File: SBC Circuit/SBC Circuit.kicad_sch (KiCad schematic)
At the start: 21 parts, among them J3 Conn_01x06_Pin, SW1 RESET, U1 MC68000FN, U11 MC34064P, X1 SG-531

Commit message: Assign Footprints
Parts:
- C10, C11, C12, C13, C14, C15, C5, C6, C7, C8, C9: footprint (none) -> Capacitor_THT:CP_Box_L5.50mm_W4.00mm_P2.50mm_NonPolarized
- J3: footprint (none) -> Connector_PinHeader_2.54mm:PinHeader_1x06_P2.54mm_Vertical
- R2, R3, R4: footprint (none) -> Resistor_THT:R_Axial_DIN0204_L3.6mm_D1.6mm_P2.54mm_Vertical
- SW1: footprint (none) -> Button_Switch_THT:SW_PUSH_6mm
- TP3: footprint (none) -> TestPoint:TestPoint_Keystone_5000-5004_Miniature
- U1: footprint Package_LCC:PLCC-68 -> Package_LCC:PLCC-68_THT-Socket
- U11: footprint Package_TO_SOT_THT:TO-92L_Inline -> Package_TO_SOT_THT:TO-92_Inline
- U2: value ~ -> XC9572XL; footprint (none) -> Package_LCC:PLCC-44_THT-Socket; Role XC9572XL -> (none)
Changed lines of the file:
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@@
       (effects (font (size 1.27 1.27)) (justify left))
     )
-    (property "Value" "~" (at 102.87 139.7 0)
-      (effects (font (size 1.27 1.27)))
-    )
-    (property "Footprint" "" (at 102.87 139.7 0)
+    (property "Value" "XC9572XL" (at 102.87 139.7 0)
+      (effects (font (size 1.27 1.27)))
+    )
+    (property "Footprint" "Package_LCC:PLCC-44_THT-Socket" (at 102.87 139.7 0)
       (effects (font (size 1.27 1.27)) hide)
     )
     (property "Datasheet" "" (at 102.87 139.7 0)
       (effects (font (size 1.27 1.27)) hide)
-    )
-    (property "Role" "XC9572XL" (at 102.87 139.7 0)
-      (effects (font (size 1.27 1.27)))
     )
     (property "Role2" "ADDRESS ROUTER" (at 102.87 142.24 0)
@@
       (effects (font (size 1.27 1.27)) (justify left))
     )
-    (property "Footprint" "" (at 117.602 34.29 90)
+    (property "Footprint" "Resistor_THT:R_Axial_DIN0204_L3.6mm_D1.6mm_P2.54mm_Vertical" (at 117.602 34.29 90)
       (effects (font (size 1.27 1.27)) hide)
     )
@@
       (effects (font (size 1.27 1.27)))
     )
-    (property "Footprint" "" (at 79.0448 85.09 0)
+    (property "Footprint" "Capacitor_THT:CP_Box_L5.50mm_W4.00mm_P2.50mm_NonPolarized" (at 79.0448 85.09 0)
       (effects (font (size 1.27 1.27)) hide)
     )
@@
       (effects (font (size 1.27 1.27)))
     )
-    (property "Footprint" "" (at 239.7252 19.05 0)
+    (property "Footprint" "Capacitor_THT:CP_Box_L5.50mm_W4.00mm_P2.50mm_NonPolarized" (at 239.7252 19.05 0)
       (effects (font (size 1.27 1.27)) hide)
     )
@@
       (effects (font (size 1.27 1.27)) (justify left))
     )
-    (property "Footprint" "" (at 88.9 50.8 0)
+    (property "Footprint" "Button_Switch_THT:SW_PUSH_6mm" (at 88.9 50.8 0)
       (effects (font (size 1.27 1.27)) hide)
     )
@@
       (effects (font (size 1.27 1.27)))
     )
-    (property "Footprint" "Package_TO_SOT_THT:TO-92L_Inline" (at 106.68 55.88 0)
+    (property "Footprint" "Package_TO_SOT_THT:TO-92_Inline" (at 106.68 55.88 0)
       (effects (font (size 1.27 1.27)) hide)
     )
@@
       (effects (font (size 1.27 1.27)))
     )
-    (property "Footprint" "" (at 119.6848 85.09 0)
+    (property "Footprint" "Capacitor_THT:CP_Box_L5.50mm_W4.00mm_P2.50mm_NonPolarized" (at 119.6848 85.09 0)
       (effects (font (size 1.27 1.27)) hide)
     )
@@
       (effects (font (size 1.27 1.27)))
     )
-    (property "Footprint" "" (at 212.3948 19.05 0)
+    (property "Footprint" "Capacitor_THT:CP_Box_L5.50mm_W4.00mm_P2.50mm_NonPolarized" (at 212.3948 19.05 0)
       (effects (font (size 1.27 1.27)) hide)
     )
@@
       (effects (font (size 1.27 1.27)) (justify left))
     )
-    (property "Footprint" "" (at 120.3452 53.34 0)
+    (property "Footprint" "Capacitor_THT:CP_Box_L5.50mm_W4.00mm_P2.50mm_NonPolarized" (at 120.3452 53.34 0)
       (effects (font (size 1.27 1.27)) hide)
     )
@@
       (effects (font (size 1.27 1.27)) (justify left))
     )
-    (property "Footprint" "" (at 95.758 34.29 90)
+    (property "Footprint" "Resistor_THT:R_Axial_DIN0204_L3.6mm_D1.6mm_P2.54mm_Vertical" (at 95.758 34.29 90)
       (effects (font (size 1.27 1.27)) hide)
     )
@@
       (effects (font (size 1.27 1.27)) (justify left))
     )
-    (property "Footprint" "" (at 54.61 38.1 0)
+    (property "Footprint" "Connector_PinHeader_2.54mm:PinHeader_1x06_P2.54mm_Vertical" (at 54.61 38.1 0)
       (effects (font (size 1.27 1.27)) hide)
     )
@@
       (effects (font (size 1.27 1.27)))
     )
-    (property "Footprint" "" (at 232.7148 19.05 0)
+    (property "Footprint" "Capacitor_THT:CP_Box_L5.50mm_W4.00mm_P2.50mm_NonPolarized" (at 232.7148 19.05 0)
       (effects (font (size 1.27 1.27)) hide)
     )
@@
       (effects (font (size 1.27 1.27)))
     )
-    (property "Footprint" "" (at 106.3752 85.09 0)
+    (property "Footprint" "Capacitor_THT:CP_Box_L5.50mm_W4.00mm_P2.50mm_NonPolarized" (at 106.3752 85.09 0)
       (effects (font (size 1.27 1.27)) hide)
     )
@@
       (effects (font (size 1.27 1.27)))
     )
-    (property "Footprint" "" (at 126.6952 85.09 0)
+    (property "Footprint" "Capacitor_THT:CP_Box_L5.50mm_W4.00mm_P2.50mm_NonPolarized" (at 126.6952 85.09 0)
       (effects (font (size 1.27 1.27)) hide)
     )
@@
       (effects (font (size 1.27 1.27)))
     )
-    (property "Footprint" "" (at 189.23 142.748 90)
+    (property "Footprint" "Resistor_THT:R_Axial_DIN0204_L3.6mm_D1.6mm_P2.54mm_Vertical" (at 189.23 142.748 90)
       (effects (font (size 1.27 1.27)) hide)
     )
@@
       (effects (font (size 1.27 1.27)))
     )
-    (property "Footprint" "" (at 99.3648 85.09 0)
+    (property "Footprint" "Capacitor_THT:CP_Box_L5.50mm_W4.00mm_P2.50mm_NonPolarized" (at 99.3648 85.09 0)
       (effects (font (size 1.27 1.27)) hide)
     )
@@
       (effects (font (size 1.27 1.27)))
     )
-    (property "Footprint" "Package_LCC:PLCC-68" (at 207.01 46.99 0)
+    (property "Footprint" "Package_LCC:PLCC-68_THT-Socket" (at 207.01 46.99 0)
       (effects (font (size 1.27 1.27)) hide)
     )
@@
       (effects (font (size 1.27 1.27)))
     )
-    (property "Footprint" "" (at 219.4052 19.05 0)
+    (property "Footprint" "Capacitor_THT:CP_Box_L5.50mm_W4.00mm_P2.50mm_NonPolarized" (at 219.4052 19.05 0)
       (effects (font (size 1.27 1.27)) hide)
     )
@@
       (effects (font (size 1.27 1.27)) (justify left))
     )
-    (property "Footprint" "" (at 134.62 38.1 0)
+    (property "Footprint" "TestPoint:TestPoint_Keystone_5000-5004_Miniature" (at 134.62 38.1 0)
       (effects (font (size 1.27 1.27)) hide)
     )
@@
       (effects (font (size 1.27 1.27)))
     )
-    (property "Footprint" "" (at 86.0552 85.09 0)
-      (effects (font (size 1.27 1.27)) hide)
-    )
+    (property "Footprint" "Capacitor_THT:CP_Box_L5.50mm_W4.00mm_P2.50mm_NonPolarized" (at 86.0552 85.09 0)
+      (effects (font (size 1.27 1.27)) hide)
+    )

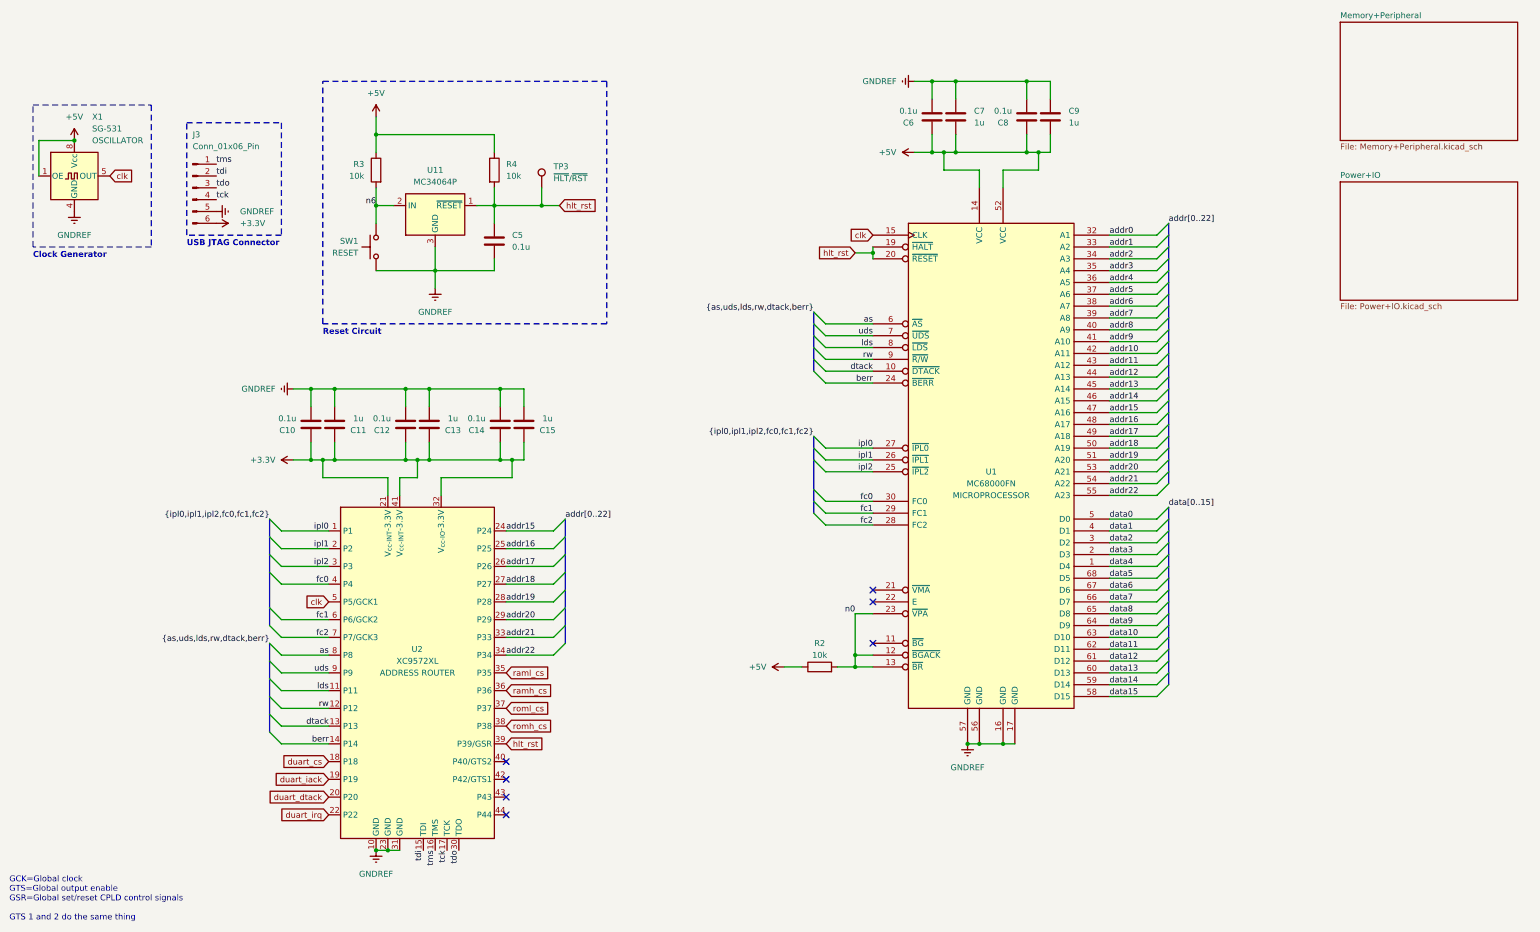
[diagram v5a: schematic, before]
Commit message: Fix intersheet bus issues
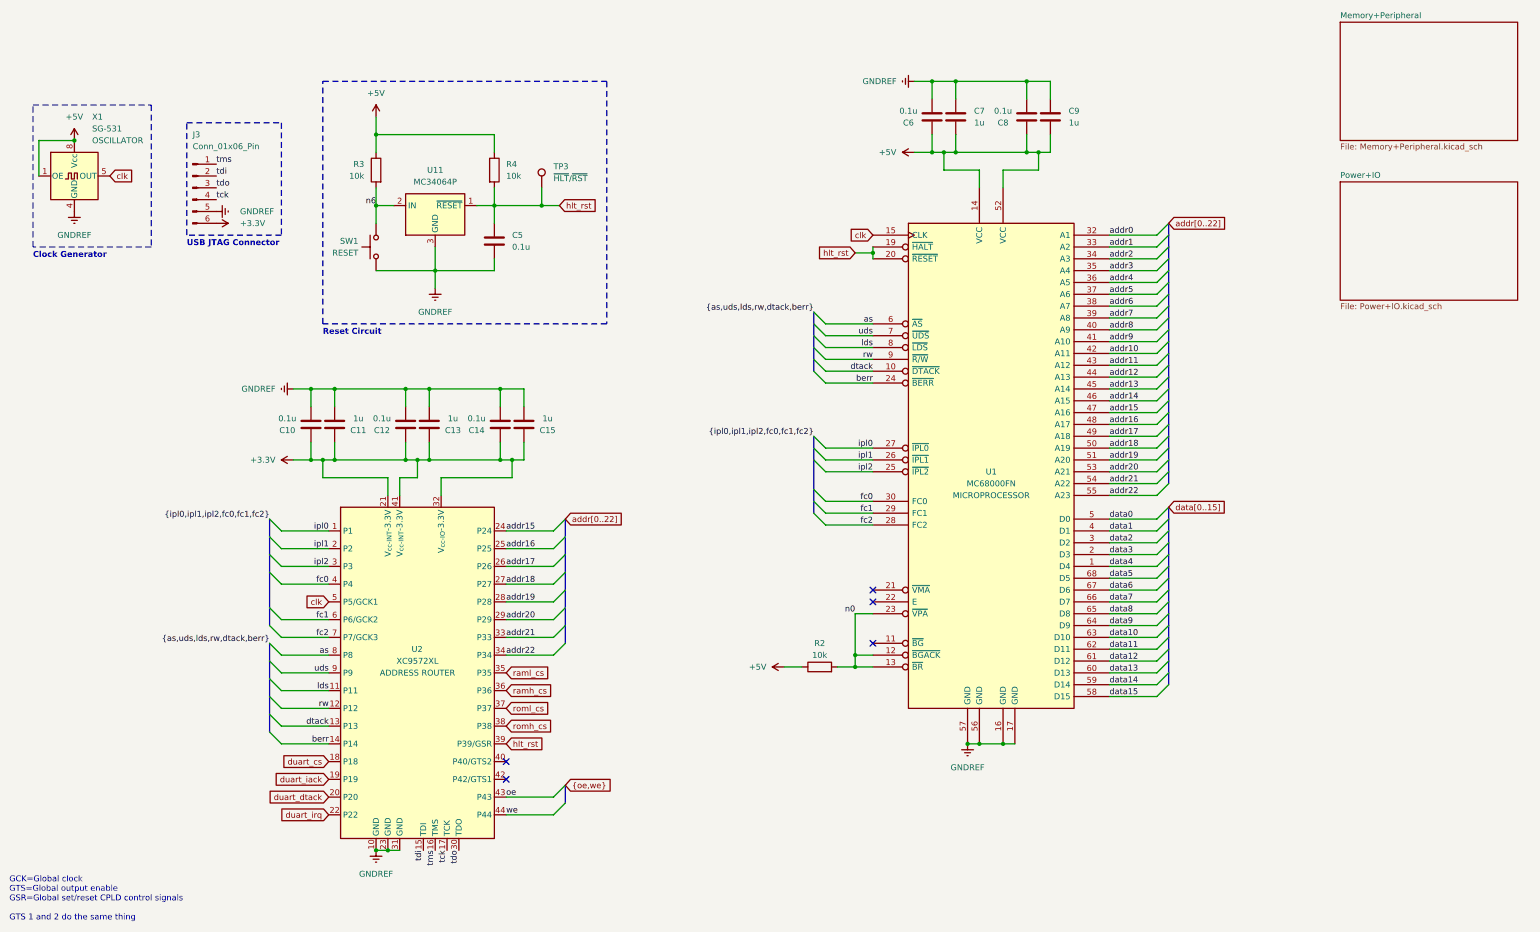
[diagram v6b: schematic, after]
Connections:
- net oe: now reaches U2.43 (P43)
- net we: now reaches U2.44 (P44)
- no-connect marks 7 -> 5

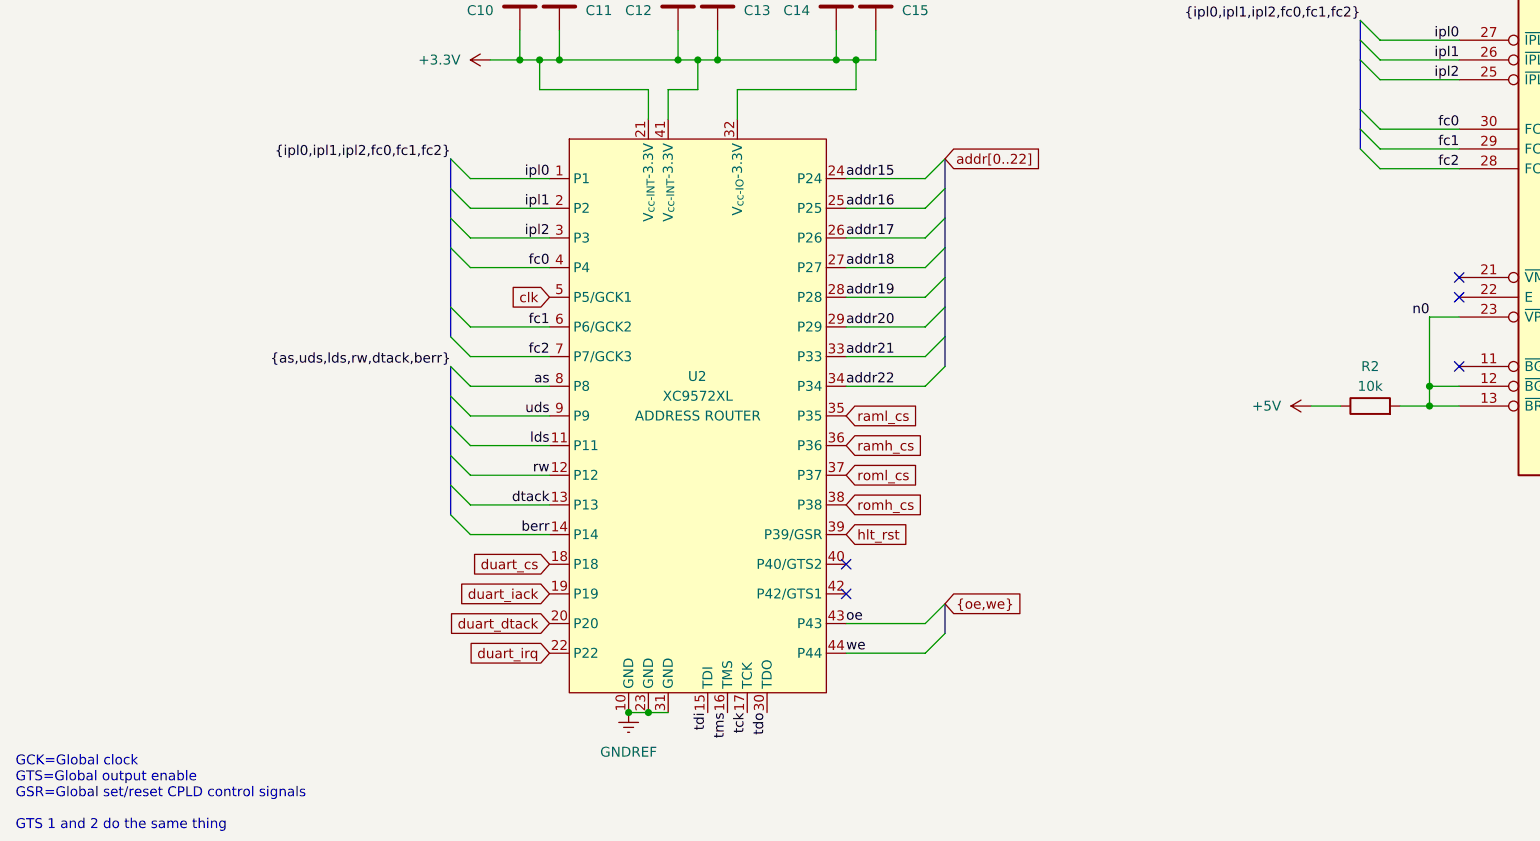
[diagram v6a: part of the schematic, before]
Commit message: PCB CPLD to MPU lines wired
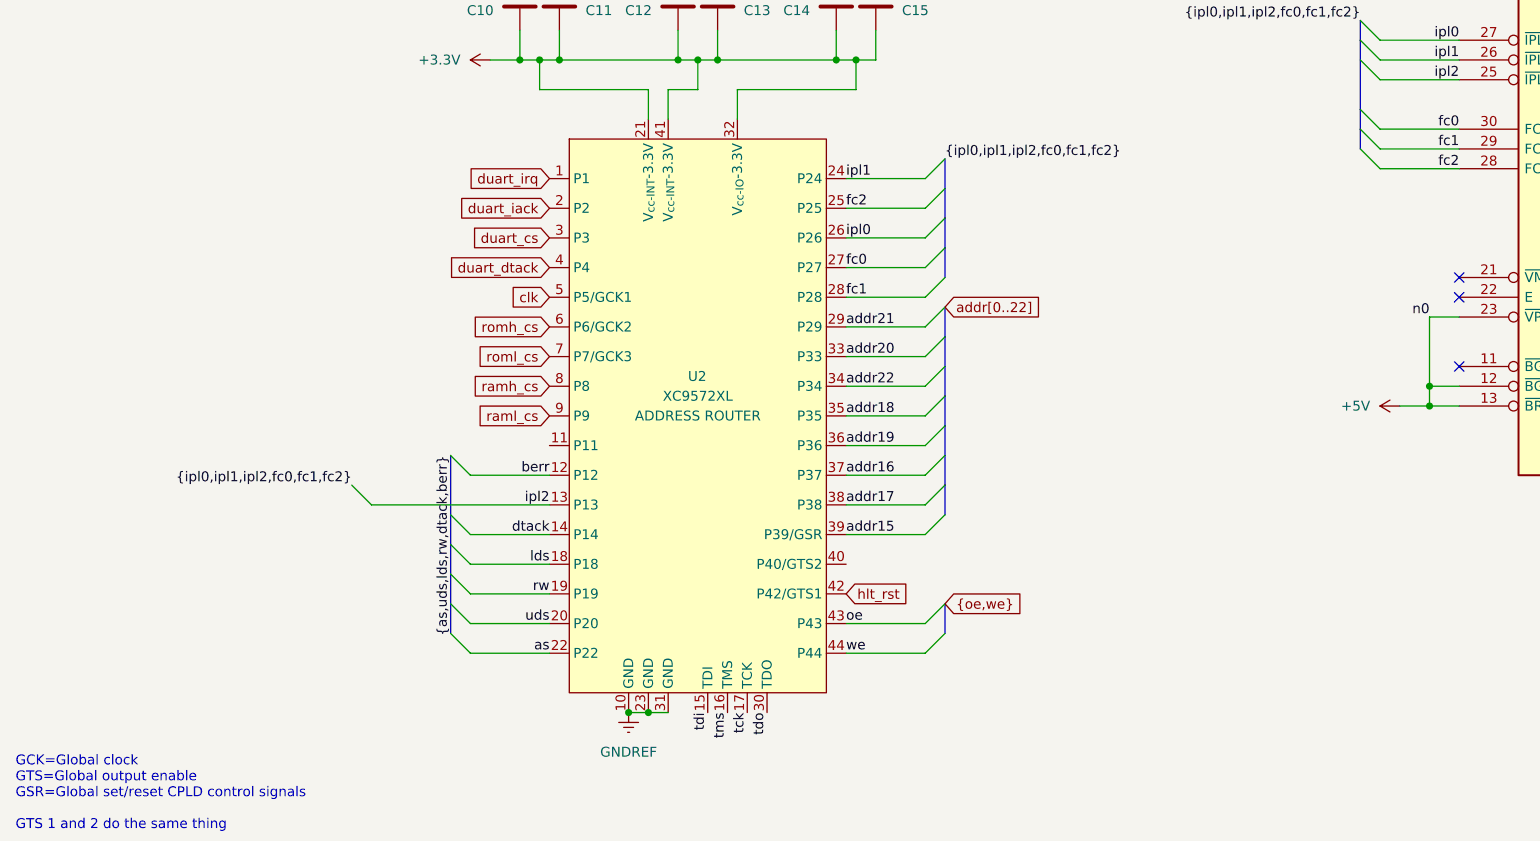
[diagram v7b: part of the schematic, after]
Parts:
- removed R2: 10k, Resistor_THT:R_Axial_DIN0204_L3.6mm_D1.6mm_P2.54mm_Vertical, symbol Device:R
- C10, C11, C12, C13, C14, C15, C5, C6, C7, C8, C9: footprint Capacitor_THT:CP_Box_L5.50mm_W4.00mm_P2.50mm_NonPolarized -> Capacitor_THT:CP_Disc_L5.50mm_W4.00mm_P2.50mm_NonPolarized
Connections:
- net n0 is gone; now on net +5V: U1.12 (~{BGACK}), U1.13 (~{BR}), U1.23 (~{VPA})
- net addr15: now also U2.39 (P39/GSR); no longer U2.24 (P24)
- net addr16: now also U2.37 (P37); no longer U2.25 (P25)
- net addr17: now also U2.38 (P38); no longer U2.26 (P26)
- net addr18: now also U2.35 (P35); no longer U2.27 (P27)
- net addr19: now also U2.36 (P36); no longer U2.28 (P28)
- net addr20: now also U2.33 (P33); no longer U2.29 (P29)
- net addr21: now also U2.29 (P29); no longer U2.33 (P33)
- net as: now also U2.22 (P22); no longer U2.8 (P8)
- net berr: now also U2.12 (P12); no longer U2.14 (P14)
- net dtack: now also U2.14 (P14); no longer U2.13 (P13)
- net duart_cs: now also U2.3 (P3); no longer U2.18 (P18)
- net duart_dtack: now also U2.4 (P4); no longer U2.20 (P20)
- net duart_iack: now also U2.2 (P2); no longer U2.19 (P19)
- net duart_irq: now also U2.1 (P1); no longer U2.22 (P22)
- net fc0: now also U2.27 (P27); no longer U2.4 (P4)
- net fc1: now also U2.28 (P28); no longer U2.6 (P6/GCK2)
- net fc2: now also U2.25 (P25); no longer U2.7 (P7/GCK3)
- net hlt_rst: now also U2.42 (P42/GTS1); no longer U2.39 (P39/GSR)
- net ipl0: now also U2.26 (P26); no longer U2.1 (P1)
- net ipl1: now also U2.24 (P24); no longer U2.2 (P2)
- net ipl2: now also U2.13 (P13); no longer U2.3 (P3)
- net lds: now also U2.18 (P18); no longer U2.11 (P11)
- net ramh_cs: now also U2.8 (P8); no longer U2.36 (P36)
- net raml_cs: now also U2.9 (P9); no longer U2.35 (P35)
- net romh_cs: now also U2.6 (P6/GCK2); no longer U2.38 (P38)
- net roml_cs: now also U2.7 (P7/GCK3); no longer U2.37 (P37)
- net rw: now also U2.19 (P19); no longer U2.12 (P12)
- net uds: now also U2.20 (P20); no longer U2.9 (P9)
- no-connect marks 5 -> 3
